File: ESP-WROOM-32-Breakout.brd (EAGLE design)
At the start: 35.6 x 40.6 mm, 10 parts, among them SW1 PROG, SW2 RST, U3 ESP-WROOM-32

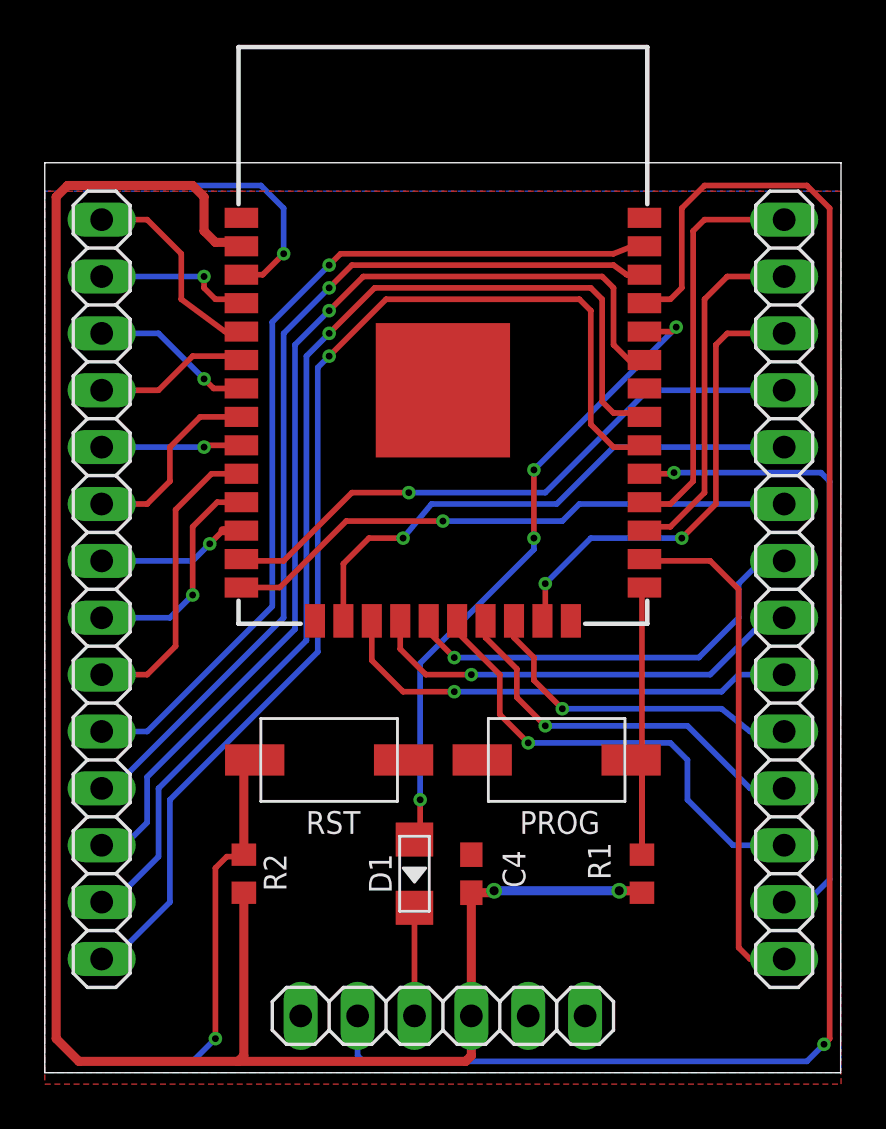
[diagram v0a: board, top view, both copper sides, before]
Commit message: smaller header pads reduced board size added mounting holes stitching via’s at antenna
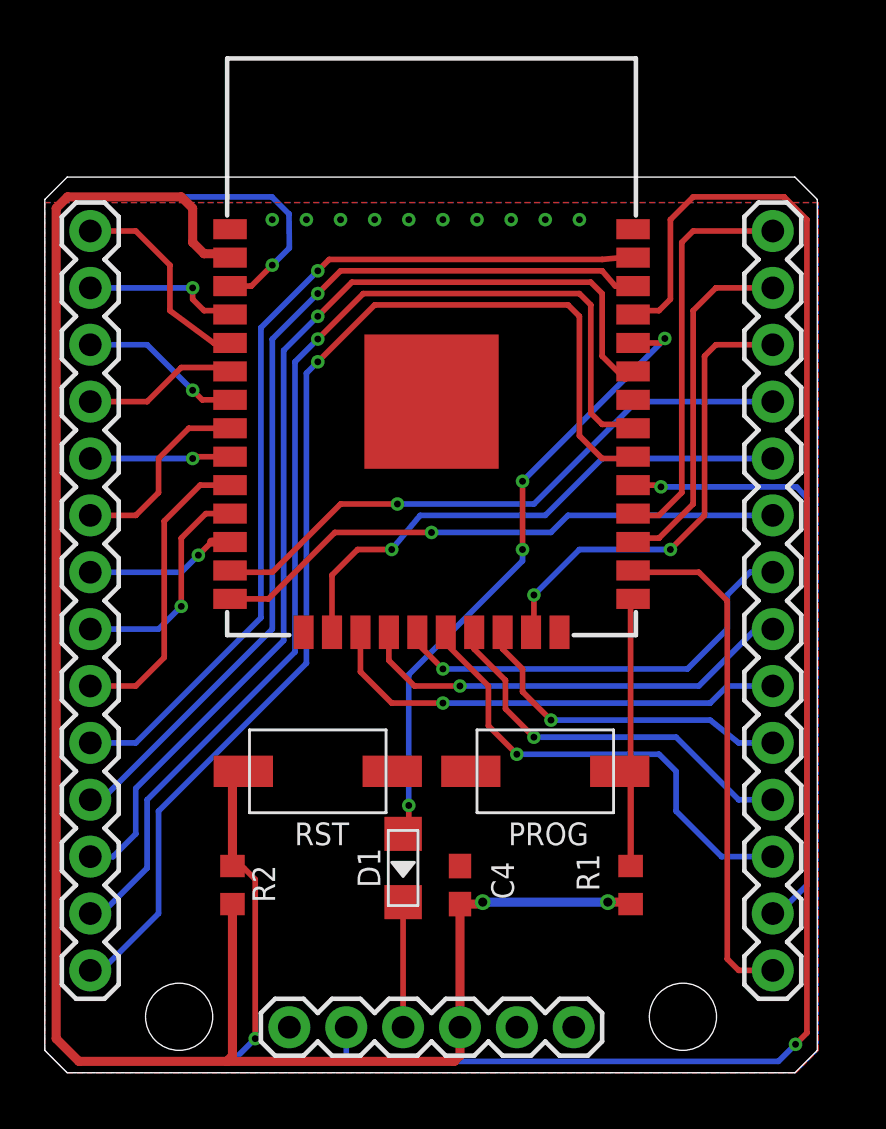
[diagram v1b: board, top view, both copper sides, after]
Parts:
- JP1, JP2: device pinhead:1X14 -> SparkFun-Connectors:1X14
- JP3: device pinhead:1X06 -> SparkFun-Connectors:1X06
- moved JP1 17.0 mm to (2.03, 4.57), turned to 90 degrees
- moved JP2 17.0 mm to (32.5, 4.57), turned to 90 degrees
- moved JP3 6.88 mm to (10.9, 2.03)
- moved R1 0.72 mm to (26.2, 8.38)
- moved R2 0.72 mm to (8.38, 8.38)
- moved U3 0.72 mm to (17.3, 30.0)
- moved C4 0.72 mm to (18.5, 8.38)
- moved SW1 0.72 mm to (22.4, 13.5)
- moved SW2 0.72 mm to (12.2, 13.5)
- moved D1 0.57 mm to (16.0, 9.14)
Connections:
- net IO10: now also JP2.7; no longer JP2.8
- net IO11: now also JP2.8; no longer JP2.7
- net IO12: now also JP2.9; no longer JP2.6
- net IO13: now also JP2.10; no longer JP2.5
- net IO14: now also JP2.11; no longer JP2.4
- net IO15: now also JP2.12; no longer JP2.3
- net IO16: now also JP2.13; no longer JP2.2
- net IO17: now also JP2.14; no longer JP2.1
- net IO18: now also JP1.1; no longer JP1.14
- net IO19: now also JP1.2; no longer JP1.13
- net IO21: now also JP1.3; no longer JP1.12
- net IO22: now also JP1.4; no longer JP1.11
- net IO23: now also JP1.5; no longer JP1.10
- net IO25: now also JP1.6; no longer JP1.9
- net IO26: now also JP1.7; no longer JP1.8
- net IO27: now also JP1.8; no longer JP1.7
- net IO32: now also JP1.9; no longer JP1.6
- net IO33: now also JP1.10; no longer JP1.5
- net IO34: now also JP1.11; no longer JP1.4
- net IO35: now also JP1.12; no longer JP1.3
- net IO36: now also JP1.13; no longer JP1.2
- net IO39: now also JP1.14; no longer JP1.1
- net IO4: now also JP2.1; no longer JP2.14
- net IO5: now also JP2.2; no longer JP2.13
- net IO6: now also JP2.3; no longer JP2.12
- net IO7: now also JP2.4; no longer JP2.11
- net IO8: now also JP2.5; no longer JP2.10
- net IO9: now also JP2.6; no longer JP2.9
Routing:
- net VCC: track 89.8 -> 87.2 mm
- net TXD0: track 73.4 -> 71.2 mm
- net EN: track 74.2 -> 75.6 mm
- net IO5: track 28.7 -> 27.4 mm
- net RX: track 4.83 -> 5.59 mm
- net IO18: track 52.3 -> 52.8 mm
- net IO21: track 46.7 -> 47.2 mm
- net IO19: track 49.9 -> 50.4 mm
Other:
- board size 35.6 x 40.6 mm -> 34.5 x 40 mm

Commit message: improved silks
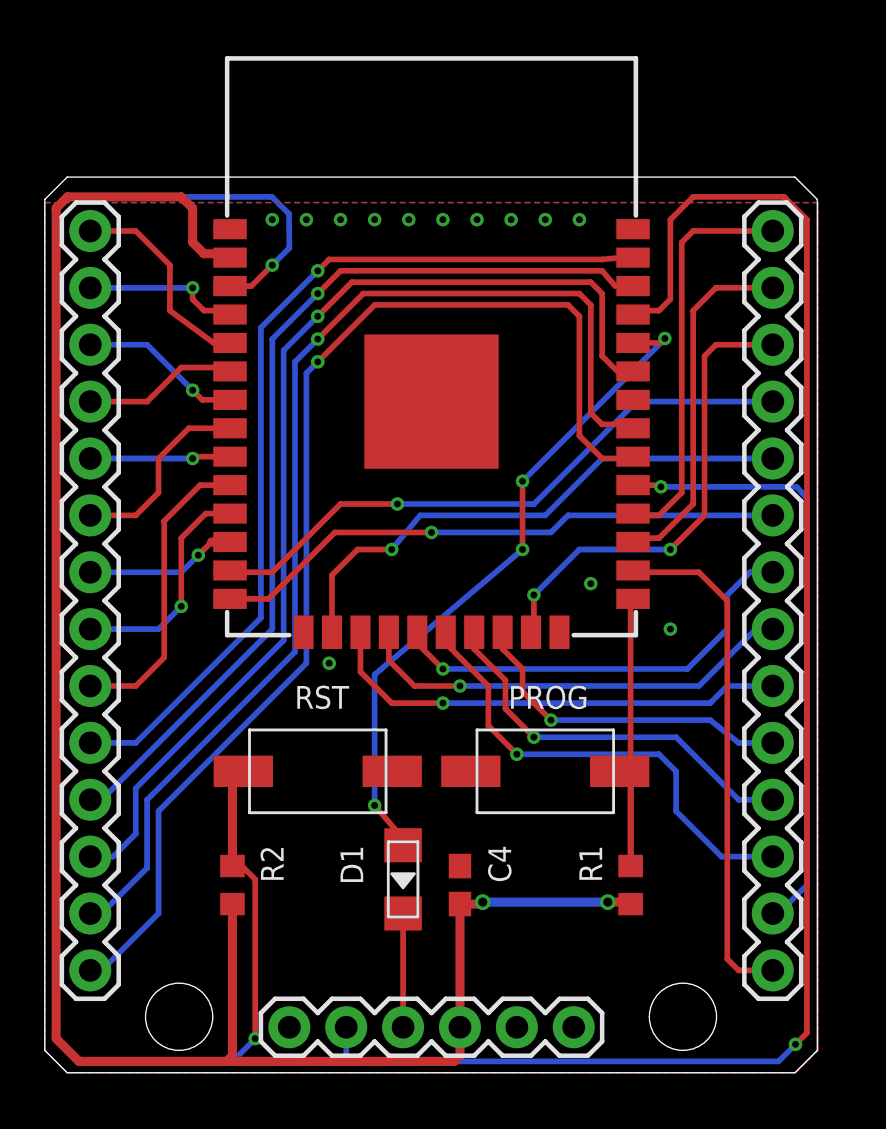
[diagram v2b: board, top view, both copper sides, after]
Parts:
- moved D1 0.51 mm to (16.0, 8.64)
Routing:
- net RXD0: track 29.4 -> 30.6 mm
- net RX: track 5.59 -> 5.08 mm
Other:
- board text added: "By Studio Sophisti"
- board text added: "ESP-WROOM-32 Breakout"
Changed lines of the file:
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@@
 <hole x="6" y="2.5" drill="3"/>
 <hole x="28.5" y="2.5" drill="3"/>
+<text x="17.272" y="29.972" size="1.016" layer="52" font="vector" ratio="12" rot="MR0" align="bottom-center">ESP-WROOM-32 Breakout</text>
+<text x="17.272" y="27.94" size="1.016" layer="52" font="vector" ratio="12" rot="MR0" align="bottom-center">By Studio Sophisti</text>
 </plain>
 <attributes>
@@
 <elements>
 <element name="C4" library="rcl" package="C0603" value="10u" x="18.542" y="8.382" smashed="yes" rot="R90">
-<attribute name="NAME" x="20.955" y="7.747" size="1.016" layer="25" font="vector" ratio="12" rot="R90"/>
+<attribute name="NAME" x="20.828" y="10.16" size="1.016" layer="25" font="vector" ratio="12" rot="R90" align="bottom-right"/>
 </element>
 <element name="R2" library="rcl" package="R0603" value="10k" x="8.382" y="8.382" smashed="yes" rot="R270">
-<attribute name="NAME" x="9.271" y="9.271" size="1.016" layer="25" font="vector" ratio="12" rot="R270"/>
+<attribute name="NAME" x="9.652" y="10.16" size="1.016" layer="25" font="vector" ratio="12" rot="R270"/>
 </element>
 <element name="U3" library="esp32" package="ESP-WROOM-32" value="ESP-WROOM-32" x="17.272" y="29.972" smashed="yes" rot="R90">
@@
 </element>
 <element name="R1" library="rcl" package="R0603" value="10k" x="26.162" y="8.382" smashed="yes" rot="R270">
-<attribute name="NAME" x="23.749" y="9.779" size="1.016" layer="25" font="vector" ratio="12" rot="R270"/>
+<attribute name="NAME" x="23.876" y="10.16" size="1.016" layer="25" font="vector" ratio="12" rot="R270"/>
 </element>
 <element name="SW1" library="Seeed-OPL-Switch" package="SW2-4.0-6.0X3.0X2.5MM" value="PROG" x="22.352" y="13.462" smashed="yes">
-<attribute name="VALUE" x="20.701" y="10.16" size="1.016" layer="25" font="vector" ratio="12"/>
+<attribute name="VALUE" x="20.701" y="16.256" size="1.016" layer="25" font="vector" ratio="12"/>
 </element>
 <element name="SW2" library="Seeed-OPL-Switch" package="SW2-4.0-6.0X3.0X2.5MM" value="RST" x="12.192" y="13.462" smashed="yes" rot="R180">
-<attribute name="VALUE" x="13.589" y="11.176" size="1.016" layer="25" font="vector" ratio="12" rot="R180"/>
-</element>
-<element name="D1" library="Seeed-OPL-Diode" package="LL-34" value="" x="16.002" y="9.144" smashed="yes" rot="R270">
-<attribute name="NAME" x="13.97" y="10.033" size="1.016" layer="25" font="vector" ratio="12" rot="R270"/>
-<attribute name="VALUE" x="13.97" y="11.049" size="0.889" layer="27" font="vector" ratio="11" rot="R270"/>
+<attribute name="VALUE" x="13.589" y="17.272" size="1.016" layer="25" font="vector" ratio="12" rot="R180"/>
+</element>
+<element name="D1" library="Seeed-OPL-Diode" package="LL-34" value="" x="16.002" y="8.636" smashed="yes" rot="R270">
+<attribute name="NAME" x="13.208" y="10.16" size="1.016" layer="25" font="vector" ratio="12" rot="R270"/>
+<attribute name="VALUE" x="13.97" y="10.541" size="0.889" layer="27" font="vector" ratio="11" rot="R270"/>
 </element>
 <element name="JP1" library="SparkFun-Connectors" package="1X14" value="" x="2.032" y="4.572" smashed="yes" rot="R90">
@@
 <via x="22.352" y="38.1" extent="1-16" drill="0.3048"/>
 <via x="23.876" y="38.1" extent="1-16" drill="0.3048"/>
+<via x="27.94" y="19.812" extent="1-16" drill="0.3048"/>
+<via x="24.384" y="21.844" extent="1-16" drill="0.3048"/>
+<via x="12.7" y="18.288" extent="1-16" drill="0.3048"/>
 </signal>
 <signal name="VCC" class="2">
@@
 <wire x1="21.336" y1="26.416" x2="21.336" y2="23.368" width="0.254" layer="1"/>
 <via x="21.336" y="23.368" extent="1-16" drill="0.3048"/>
-<wire x1="21.336" y1="23.368" x2="21.336" y2="22.86" width="0.254" layer="16"/>
-<wire x1="21.336" y1="22.86" x2="16.256" y2="17.78" width="0.254" layer="16"/>
-<wire x1="16.256" y1="17.78" x2="16.256" y2="11.938" width="0.254" layer="16"/>
-<via x="16.256" y="11.938" extent="1-16" drill="0.3048"/>
-<wire x1="16.256" y1="11.938" x2="16.256" y2="10.16" width="0.254" layer="1"/>
-<wire x1="16.256" y1="10.16" x2="16.002" y2="10.668" width="0.254" layer="1"/>
+<wire x1="21.336" y1="23.368" x2="14.732" y2="17.78" width="0.254" layer="16"/>
+<wire x1="14.732" y1="17.78" x2="14.732" y2="11.938" width="0.254" layer="16"/>
+<via x="14.732" y="11.938" extent="1-16" drill="0.3048"/>
+<wire x1="14.732" y1="11.938" x2="16.256" y2="10.16" width="0.254" layer="1"/>
+<wire x1="16.256" y1="10.16" x2="16.002" y2="10.16" width="0.254" layer="1"/>
 </signal>
 <signal name="IO0">
@@
 <contactref element="D1" pad="C"/>
 <contactref element="JP3" pad="3"/>
-<wire x1="16.002" y1="2.032" x2="16.002" y2="7.62" width="0.254" layer="1"/>
+<wire x1="16.002" y1="2.032" x2="16.002" y2="7.112" width="0.254" layer="1"/>
 </signal>
 <signal name="IO34">
